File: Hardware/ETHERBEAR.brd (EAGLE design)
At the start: 68.6 x 53.3 mm, 95 parts, among them IC1 MC33269DT-5.0, IC2 CP2102N-A01-GQFN24, IC4 LM358D, IC5 ATMEGA328P TQFP32, IC6 W6100-LQFP, IC7 MCP24AA025E48, J1 DC_2_1MM, J2 USB-C-16P-16P, P2 ICSP:MAIN, P4 microSD, Q1 FDN340P, Q2 2N7002, U1 HY931147C-RJ45

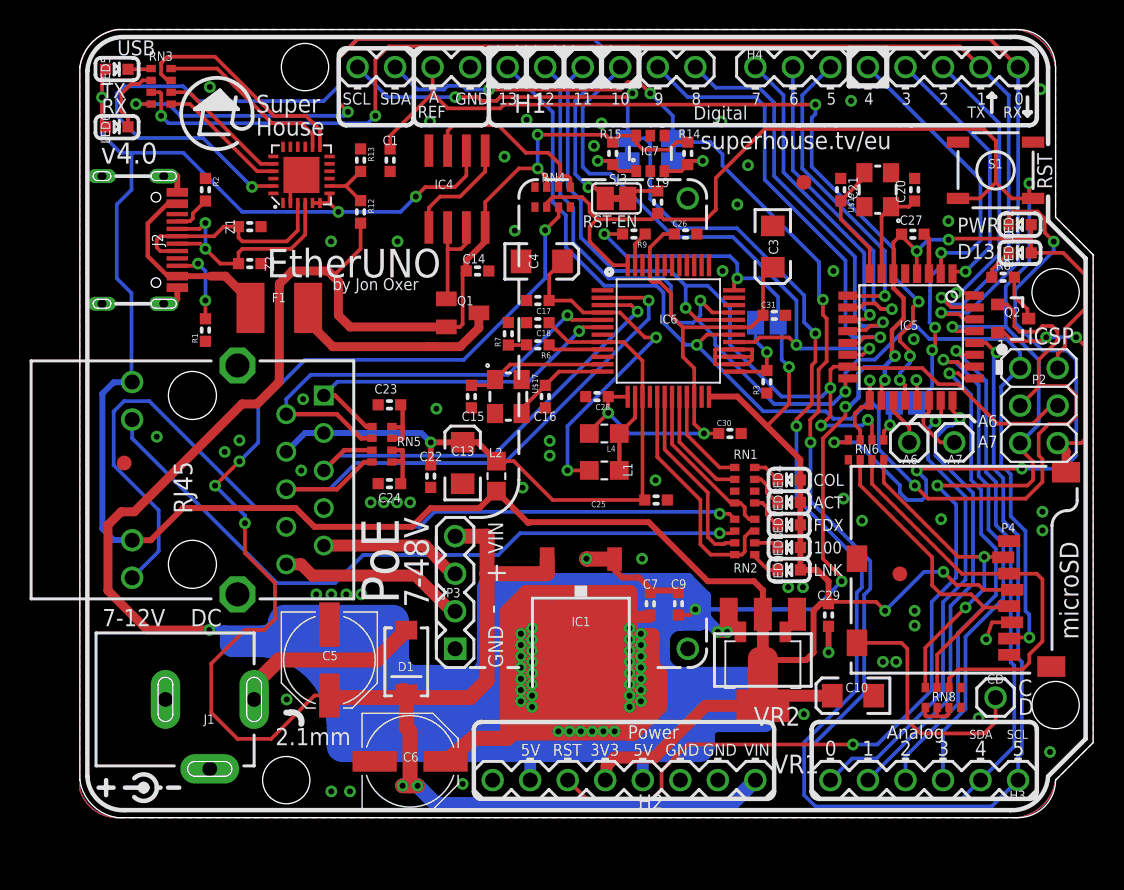
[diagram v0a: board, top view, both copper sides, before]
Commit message: Schematic changes for ATmega1284P
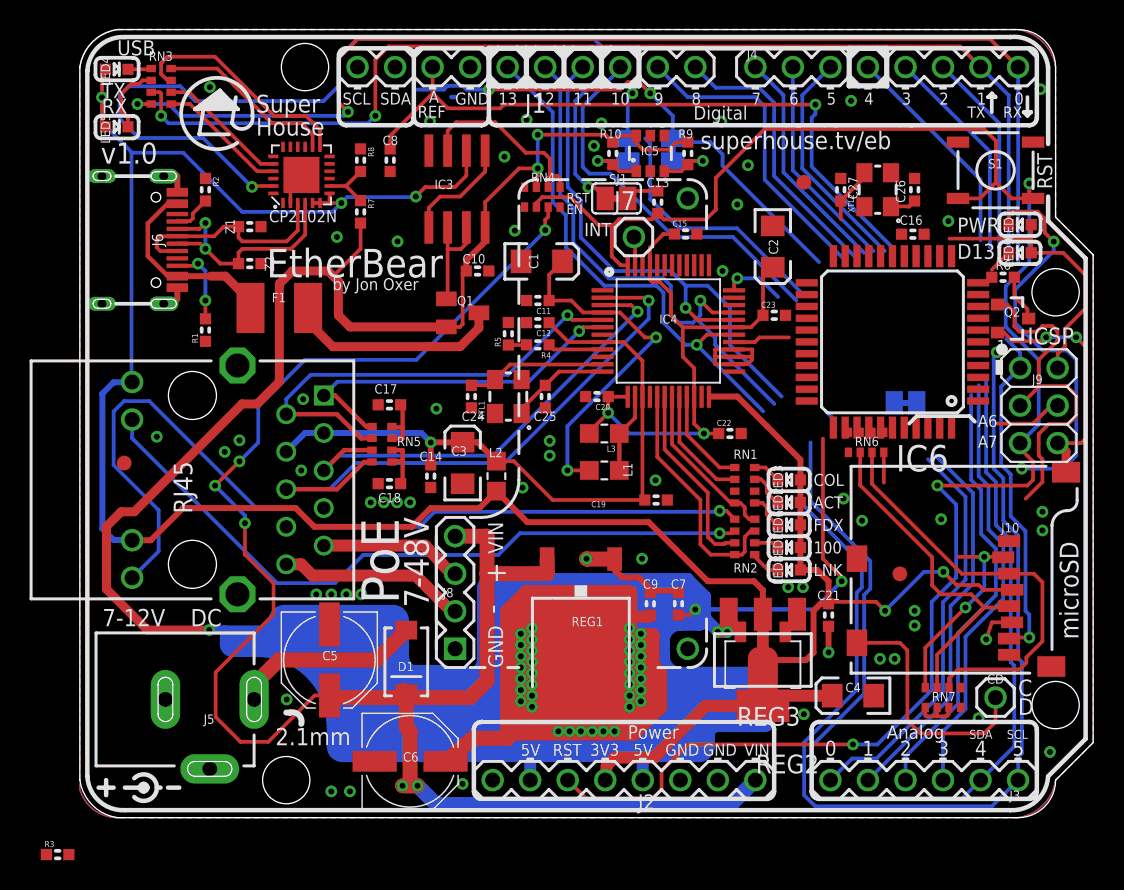
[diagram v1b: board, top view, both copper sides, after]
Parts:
- removed A6, A7: M01, SuperHouse-Connectors:1X01
- removed C28, C30, C31: 100nF, SuperHouse-DiscreteSemi:C0603
- removed C29: 100nF 0603, SuperHouse-DiscreteSemi:C0603
- removed H1: Digital_8_13, SuperHouse-Connectors:1X10-S
- removed H2: Power, SuperHouse-Connectors:1X08-S
- removed IC7: MCP24AA025E48, freetronics-jon:SOT23-6
- removed LED10: D13/RED, SuperHouse-LEDs:LED-0603
- removed R12: 22.1K, SuperHouse-DiscreteSemi:R0603
- removed R13: 47.5K, SuperHouse-DiscreteSemi:R0603
- removed R14: 4K7, SuperHouse-DiscreteSemi:R0603
- removed SJ6, SJ7: SJC, SuperHouse-Jumpers:SJC
- added C11, C12, C8: 100nF, SuperHouse-DiscreteSemi:C0603
- added C2: 10uF 6.3V A TANT, SuperHouse-DiscreteSemi:EIA3216
- added IC3: LM358D, linear:SO08
- added J5: DC_2_1MM, SuperHouse-Connectors:POWER_JACK_SLOTS
- added J6: USB-C-16P-16P, SuperHouse-Connectors:USB-C-16P
- added J7: INTERRUPT, SuperHouse-Connectors:1X01
- added LED1: PWR/BLUE, SuperHouse-LEDs:LED-0603
- added R4: 12K 1%, SuperHouse-DiscreteSemi:R0603
- added R5: 300R 1%, SuperHouse-DiscreteSemi:R0603
- added SJ1: RESET-EN, SuperHouse-Jumpers:SJC
- C1: value 100nF 0603 -> 10uF 6.3V A TANT; device SuperHouse-DiscreteSemi:C0603 -> SuperHouse-DiscreteSemi:EIA3216
- C10, C13: value 10uF 6.3V A TANT -> 100nF; device SuperHouse-DiscreteSemi:EIA3216 -> SuperHouse-DiscreteSemi:C0603
- C14, C19: value 100nF 0603 -> 100nF
- C15, C16: value 13pF -> 100nF
- C20, C21: value 22pF 0603 -> 100nF
- C24, C25: value 100nF -> 13pF
- C26: value 100nF -> 22pF
- C27: value 100nF 0603 -> 22pF
- C7: value 100nF 0603 -> 1uF
- C9: value 1uF 0603 -> 100nF
- IC4: value LM358D -> W6100-LQFP; device linear:SO08 -> SuperHouse-ICs:LQFP48
- IC5: value ATMEGA328P TQFP32 -> MCP24AA025E48; device SuperHouse-MCUs:TQFP32-08 -> freetronics-jon:SOT23-6
- IC6: value W6100-LQFP -> ATMEGA1284P-TQFP; device SuperHouse-ICs:LQFP48 -> SuperHouse-MCUs:TQFP44
- J1: value DC_2_1MM -> Digital_8_13; device SuperHouse-Connectors:POWER_JACK_SLOTS -> SuperHouse-Connectors:1X10-S
- J2: value USB-C-16P-16P -> Power; device SuperHouse-Connectors:USB-C-16P -> SuperHouse-Connectors:1X08-S
- J9: value ICSP:MAIN -> ICSP
- LED2: value PWR/BLUE -> YELLOW
- LED3: value YELLOW -> RED
- LED4: value RED -> TX/YEL
- LED5: value TX/YEL -> RX/GRN
- LED6: value RX/GRN -> GREEN
- LED8: value GREEN -> YELLOW
- LED9: value YELLOW -> D13/RED
- R6: value 12K 1% -> 1K
- R7: value 300R 1% -> 22.1K
- R8: value 1K 0603 -> 47.5K
- R9: value 10K -> 4K7
- RN1, RN2: value 330R -> 1K
- SJ3: value RESET-EN -> SJC
- SJ4: value MODE -> SJC; device SuperHouse-Jumpers:SJ -> SuperHouse-Jumpers:SJC
- XTL1: value CRYSTAL-GND3X2 -> 25MHz
- XTL2: value CRYSTAL-GND3X2 -> 16MHz
- moved R3 57.7 mm to (-1.50, -2.50), turned to 0 degrees
- moved J1 53.5 mm to (30.2, 50.8), turned to 180 degrees
- moved LED4 53.3 mm to (2.50, 50.7), turned to 0 degrees
- moved LED6 52.9 mm to (48.0, 19.8), turned to 180 degrees
- moved J2 50.8 mm to (36.8, 2.54), turned to 0 degrees
- moved R8 44.2 mm to (19.0, 44.5), turned to 270 degrees
- moved C10 38.4 mm to (26.9, 37.0), turned to 0 degrees
- moved C4 36.2 mm to (52.3, 8.26), turned to 180 degrees
- moved R6 31.8 mm to (62.5, 36.6)
- moved C21 28.8 mm to (50.7, 13.7)
- moved C16 27.2 mm to (56.4, 39.5), turned to 0 degrees
- moved C23 26.7 mm to (47.0, 34.0), turned to 0 degrees
- moved LED9 26.5 mm to (63.6, 38.2)
- moved C20 25.7 mm to (35.0, 28.5), turned to 180 degrees
- moved C3 25.6 mm to (25.9, 24.0), turned to 90 degrees
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- renumbered H3 to J3, H4 to J4, IC1 to REG1, JP3 to J8, L4 to L3, P2 to J9, P4 to J10, R15 to R10, RN8 to RN7, U$17 to XTL1, U$19 to XTL2, U1 to J11, VR1 to REG2, VR2 to REG3
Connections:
- removed net A0: IC5.23, J3.1
- removed net A1: IC5.24, J3.2
- removed net A2: IC5.25, J3.3
- removed net A3: IC5.26, J3.4
- removed net A4_SDA: H1.9, IC5.27, J3.5, SJ5.1
- removed net A5_SCL: H1.10, IC5.28, J3.6, SJ6.1
- removed net D11_MOSI: H1.4, IC5.15, IC6.32, J9.4, RN6.6
- removed net D12_MISO: H1.5, IC5.16, IC6.33, J10.7, J9.1
- removed net D2: IC5.32, J4.3
- removed net D3: IC5.1, J4.4
- removed net MODE: IC6.25, R3.2, SJ4.1
- removed net N$21: A7.1, IC5.22
- removed net N$22: A6.1, IC5.19
- removed net N$37: IC6.47, R9.1
- new net A0_D14: IC6.30, J3.1
- new net A1_D15: IC6.31, J3.2
- new net A2_D16: IC6.32, J3.3
- new net A3_D17: IC6.33, J3.4
- new net A4_D18: IC6.34, J3.5
- new net A5_D19: IC6.35, J3.6
- new net D10_SS: IC6.44
- new net D11_COPI: IC4.32, IC6.1, J1.4, J9.4, RN6.6
- new net D12_CIPO: IC4.33, IC6.2, J1.5, J10.7, J9.1
- new net D2_RX1: IC6.11, J4.3
- new net D3_TX1: IC6.12, J4.4
- new net N$9: IC4.47, J7.1, R3.2
- new net SCL: IC6.19, J1.10, SJ4.1
- new net SDA: IC6.20, J1.9, SJ3.1
- net 1V2A: now also C1.A, C11.1, IC4.4; no longer C17.1, C4.A, IC6.4
- net 1V2D: now also C15.1, C2.A, C20.1, C22.1, C23.1, IC4.13, IC4.22, IC4.31, IC4.45; no longer C26.1, C28.1, C3.A, C30.1, C31.1, IC6.13, IC6.22, IC6.31, IC6.45
- net 1V2O: now also IC4.14; no longer IC6.14
- net 3.3V: now also C21.1, C4.A, IC3.2, IC4.24, IC4.36, J2.4, LED2.A; no longer C10.A, C29.1, H2.4, IC4.2, IC6.24, IC6.36, LED9.A, R9.2, SJ4.2
- net 3V3A: now also C12.1, C14.1, C19.1, C3.A, IC4.15, IC4.8; no longer C13.A, C18.1, C22.1, C25.1, IC6.15, IC6.8
- net 5V: now also C10.1, C16.1, IC3.8, IC6.17, IC6.27, IC6.28, IC6.5, J2.2, J2.5, LED1.A, LED9.A, R3.1, R7.2, R9.1; no longer C14.1, C27.1, H2.2, H2.5, IC4.8, IC5.18, IC5.4, IC7.6, LED10.A, LED2.A, R12.2, R14.1
- net ACTLED: now also IC4.20; no longer IC6.20
- net AREF: now also C8.1, IC6.29, J1.8; no longer C1.1, H1.8, IC5.20
- net COLLED: now also IC4.21; no longer IC6.21
- net D+: now also J6.A6, J6.B6; no longer J2.A6, J2.B6
- net D-: now also J6.A7, J6.B7; no longer J2.A7, J2.B7
- net D0_RX: now also IC6.9; no longer IC5.30
- net D10_CS: now also IC4.29, J1.3; no longer H1.3, IC5.14, IC6.29
- net D13_SCK: now also IC4.30, IC6.3, J1.6; no longer H1.6, IC5.17, IC6.30
- net D1_TX: now also IC6.10; no longer IC5.31
- net D4: now also IC6.40, SJ5.2; no longer IC5.2, SJ7.2
- net D5: now also IC6.41; no longer IC5.9
- net D6: now also IC6.42; no longer IC5.10
- net D7: now also IC6.43; no longer IC5.11
- net D8: now also IC6.14, J1.1; no longer H1.1, IC5.12
- net D9: now also IC6.15, J1.2; no longer H1.2, IC5.13
- net DTR: now also SJ1.1; no longer SJ3.1
- net FDXLED: now also IC4.19; no longer IC6.19
- net GND: now also C1.C, C10.2, C11.2, C12.2, C19.2, C2.C, C20.2, C21.2, C26.1, C27.1, C8.2, IC3.4, IC4.1, IC4.10, IC4.16, IC4.23, IC4.25, IC4.26, IC4.27, IC4.28, IC4.46, IC4.7, IC5.2, IC5.4, IC6.18, IC6.38, IC6.39, IC6.6, J1.7, J2.6, J2.7, J5.GND, J5.GNDBREAK, J6.A12B1, J6.A1B12, J6.FIX1, J6.FIX2, J6.FIX3, J6.FIX4, R5.2, R8.1; no longer C1.2, C10.C, C13.C, C20.1, C21.1, C26.2, C27.2, C28.2, C29.2, C30.2, C31.2, H1.7, H2.6, H2.7, IC4.4, IC5.21, IC5.3, IC6.1, IC6.10, IC6.16, IC6.23, IC6.26, IC6.27, IC6.28, IC6.46, IC6.7, IC7.2, IC7.4, IC7.5, J1.GND, J1.GNDBREAK, J2.A12B1, J2.A1B12, J2.FIX1, J2.FIX2, J2.FIX3, J2.FIX4, R13.1, R3.1, R7.2
- net LINKLED: now also IC4.17; no longer IC6.17
- net N$1: now also C18.1; no longer C24.1
- net N$10: now also J6.B5; no longer J2.B5
- net N$11: now also LED5.C; no longer LED6.C
- net N$115: now also J6.A4B9, J6.A9B4; no longer J2.A4B9, J2.A9B4
- net N$12: now also IC3.3; no longer IC4.3
- net N$13: now also LED4.C; no longer LED5.C
- net N$14: now also LED1.C; no longer LED2.C
- net N$18: now also IC3.6, IC3.7; no longer IC4.6, IC4.7
- net N$19: now also IC3.1, IC3.5; no longer IC4.1, IC4.5
- net N$2: now also C26.2, IC6.8; no longer C20.2, IC5.7
- net N$26: now also LED7.C; no longer LED8.C
- net N$27: now also SJ5.1; no longer SJ7.1
- net N$28: now also LED8.C; no longer LED9.C
- net N$29: now also IC5.3, R9.2, SJ3.2; no longer IC7.3, R14.2, SJ5.2
- net N$3: now also C13.1, SJ1.2; no longer C19.1, SJ3.2
- net N$30: now also C24.1, IC4.11, XTL1.3; no longer C15.1, IC6.11, XTL1.1
- net N$32: now also C25.1, IC4.12, XTL1.1; no longer C16.1, IC6.12, XTL1.3
- net N$321: now also C17.1; no longer C23.1
- net N$327: now also LED6.C; no longer LED7.C
- net N$329: now also LED2.C; no longer LED3.C
- net N$34: now also J6.A5; no longer J2.A5
- net N$35: now also R4.2, R5.1; no longer R6.2, R7.1
- net N$36: now also IC4.9, R4.1; no longer IC6.9, R6.1
- net N$39: now also R7.1, R8.2; no longer R12.1, R13.2
- net N$4: now also LED9.C, R6.2; no longer LED10.C, R8.2
- net N$5: now also IC5.1, SJ4.2; no longer IC7.1, SJ6.2
- net N$6: now also R6.1; no longer R8.1
- net N$60: now also J5.PWR; no longer J1.PWR
- net N$7: now also C27.2, IC6.7; no longer C21.2, IC5.8
- net N$8: now also LED3.C; no longer LED4.C
- net RESET: now also C13.2, IC4.48, IC6.4, J2.3; no longer C19.2, H2.3, IC5.29, IC6.48
- net RXIN: now also IC4.5; no longer IC6.5
- net RXIP: now also IC4.6; no longer IC6.6
- net SPDLED: now also IC4.18; no longer IC6.18
- net TXON: now also IC4.2; no longer IC6.2
- net TXOP: now also IC4.3; no longer IC6.3
- net VIN: now also J2.8; no longer H2.8
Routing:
- net A5_SCL: track 126.9 -> 0.00 mm, vias 5 -> 0
- net A4_SDA: track 121.1 -> 0.00 mm, vias 5 -> 0
- net A5_D19: track 0.00 -> 86.7 mm, vias 0 -> 1
- net A4_D18: track 0.00 -> 81.3 mm
- net D12_MISO: track 79.8 -> 0.00 mm, vias 3 -> 0
- net D11_MOSI: track 66.9 -> 0.00 mm, vias 4 -> 0
- net D12_CIPO: track 0.00 -> 59.9 mm, vias 0 -> 2
- net D11_COPI: track 0.00 -> 41.5 mm, vias 0 -> 1
- net A3: track 34.4 -> 0.00 mm, vias 1 -> 0
- net A2: track 33.2 -> 0.00 mm, vias 1 -> 0
- net A0: track 31.9 -> 0.00 mm, vias 1 -> 0
- net A1: track 30.8 -> 0.00 mm, vias 1 -> 0
- net A2_D16: track 0.00 -> 29.3 mm
- net A3_D17: track 0.00 -> 29.1 mm
- net D13_SCK: track 88.7 -> 60.5 mm, vias 3 -> 1
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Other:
- board text added: "CP2102N"
- board text added: "EtherBear"
- board text added: "INT"
- board text added: "RST EN"
- board text added: "SKU: EB"
- board text added: "Select "Bobuino" in the Arduino IDE"
- board text added: "superhouse.tv/eb"
- board text added: "v1.0"
- board text added: "www.superhouse.tv/eb"
- board text removed: "EtherUNO"
- board text removed: "RST-EN"
- board text removed: "SKU: EU"
- board text removed: "superhouse.tv/eu"
- board text removed: "v4.0"
- board text removed: "www.superhouse.tv/eu"
